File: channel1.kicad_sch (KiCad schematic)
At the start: 58 parts, among them IC1 TLV73325PDBVT, IC2 TLV73312PDBVT, J2 47151-1001, J3 5051101992, U1 TC358742XBG, U2 TPD8S009DSMR, U3 PCA9517ATP, Y1 7C-27.000MBB-T

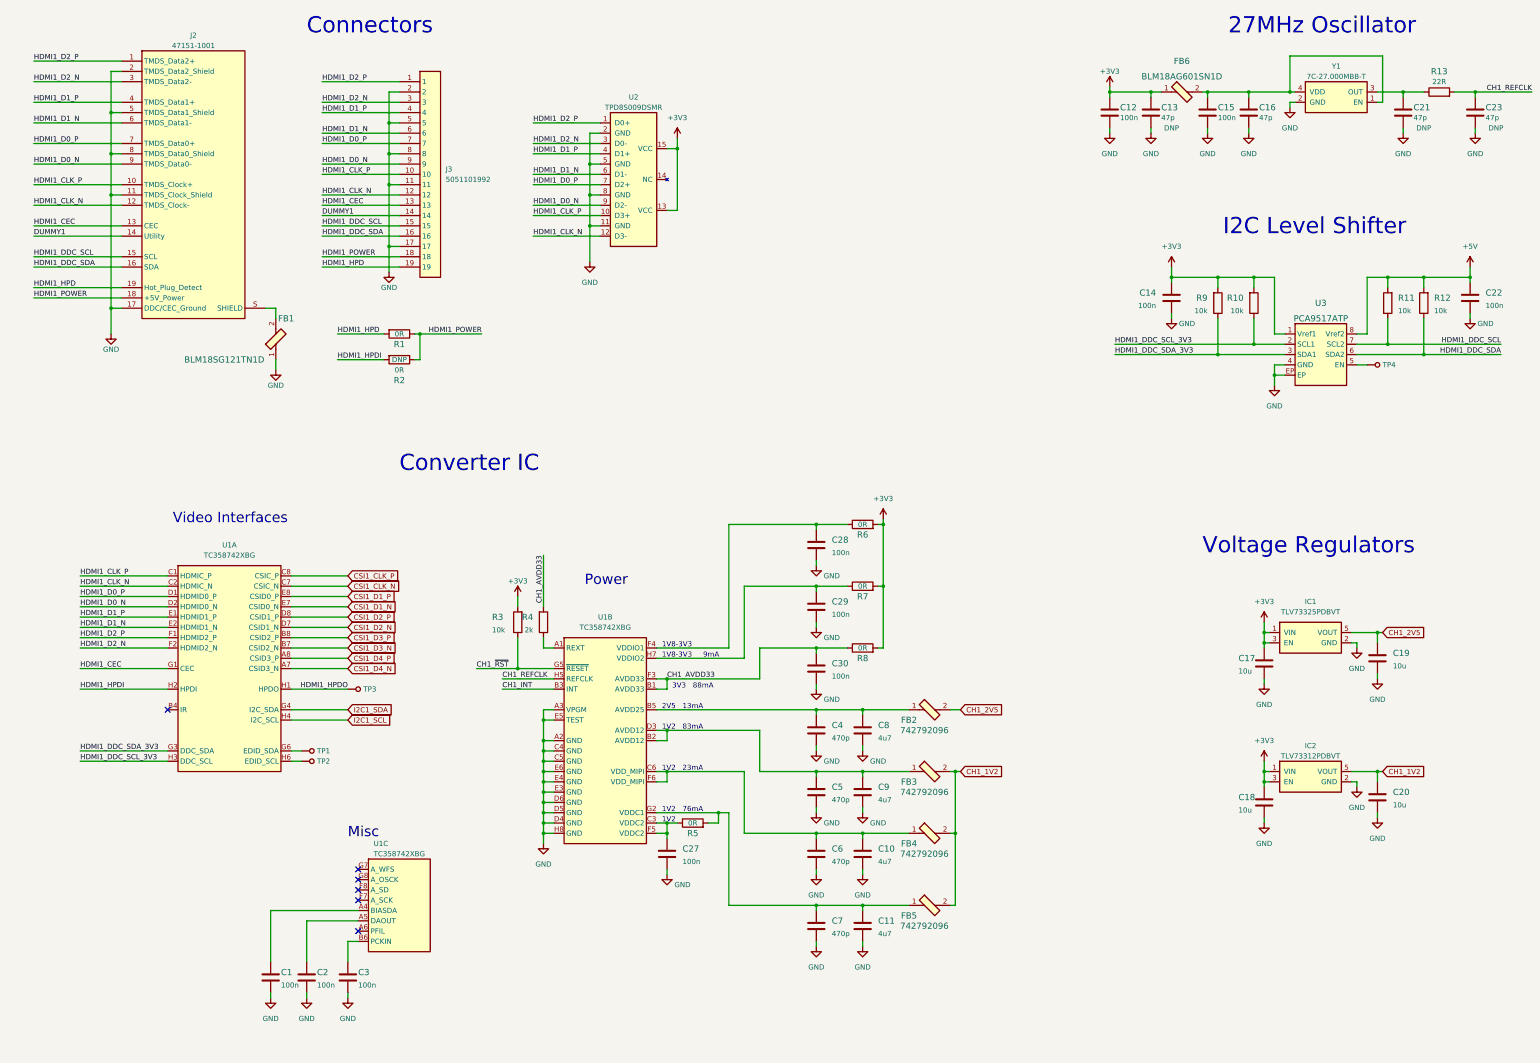
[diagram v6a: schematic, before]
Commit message: Introduce component standardization
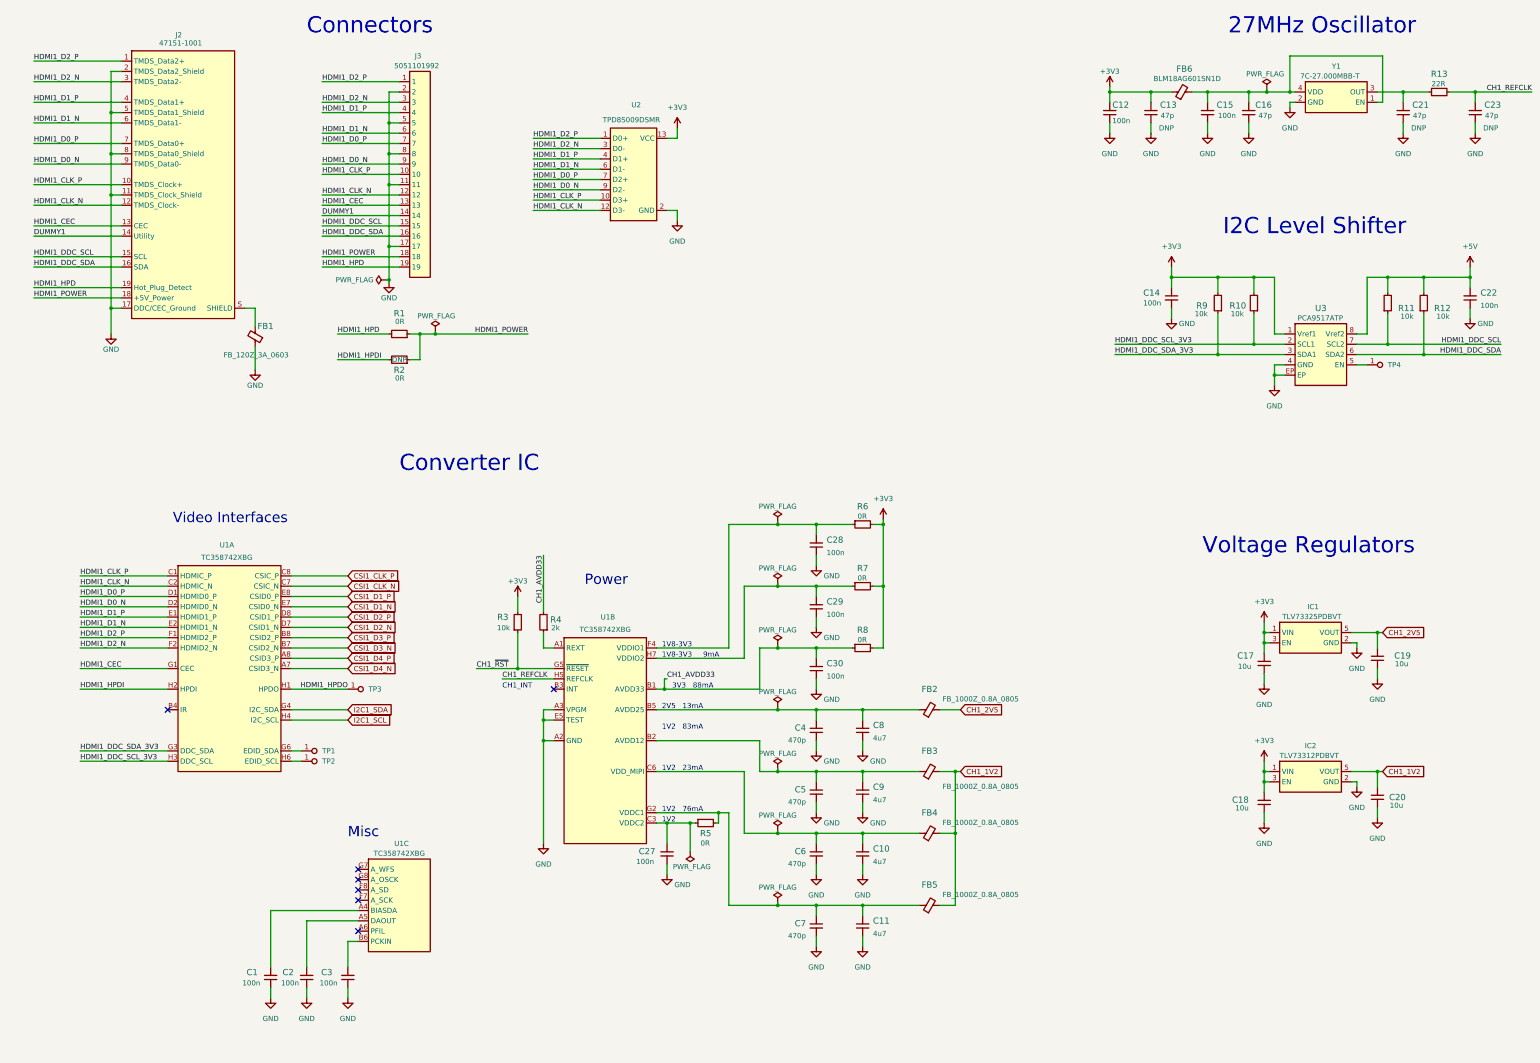
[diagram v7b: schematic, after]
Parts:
- C1, C12, C14, C15, C2, C22, C27, C28, C29, C3, C30: footprint antmicro-hdmi-mipi-bridge-hw-footprints:0402-cap -> antmicro-hdmi-mipi-bridge-hw-footprints:C_0402_1005Metric; Author (none) -> Antmicro; Dielectric (none) -> X5R; License (none) -> Apache-2.0; Voltage (none) -> 50V
- C10, C11, C17, C18, C19, C20, C8, C9: footprint antmicro-hdmi-mipi-bridge-hw-footprints:0603-cap -> antmicro-hdmi-mipi-bridge-hw-footprints:C_0603_1608Metric; Author (none) -> Antmicro; License (none) -> Apache-2.0
- C13, C16, C21, C23: footprint antmicro-hdmi-mipi-bridge-hw-footprints:0402-cap -> antmicro-hdmi-mipi-bridge-hw-footprints:C_0402_1005Metric; Author (none) -> Antmicro; Dielectric (none) -> C0G; License (none) -> Apache-2.0; MPN C0402C470J5GACTU -> GRM1555C1E470JA01D; Manufacturer KEMET -> Murata
- C4, C5, C6, C7: footprint antmicro-hdmi-mipi-bridge-hw-footprints:0402-cap -> antmicro-hdmi-mipi-bridge-hw-footprints:C_0402_1005Metric; Author (none) -> Antmicro; License (none) -> Apache-2.0; Manufacturer WALSIN -> Walsin
- FB1: value BLM18SG121TN1D -> FB_120Z_3A_0603; footprint antmicro-hdmi-mipi-bridge-hw-footprints:0603-res -> antmicro-hdmi-mipi-bridge-hw-footprints:FB_0603_1608Metric; symbol antmicro-hdmi-mipi-bridge-hw:BLM18SG121TN1D -> antmicro-hdmi-mipi-bridge-hw:FB_120Z_3A_0603; Author (none) -> Antmicro; License (none) -> Apache-2.0; Manufacturer Murata Electronics North America -> Murata
- FB2, FB3, FB4, FB5: value 742792096 -> FB_1000Z_0.8A_0805; footprint antmicro-hdmi-mipi-bridge-hw-footprints:0805-res -> antmicro-hdmi-mipi-bridge-hw-footprints:FB_0805_2012Metric; symbol antmicro-hdmi-mipi-bridge-hw:742792096 -> antmicro-hdmi-mipi-bridge-hw:FB_1000Z_0.8A_0805; Author (none) -> Antmicro; License (none) -> Apache-2.0; Manufacturer Wurth Electronic -> Würth Elektronik
- FB6: value BLM18AG601SN1D -> FB_600Z_0.5A_0603; footprint antmicro-hdmi-mipi-bridge-hw-footprints:0603 -> antmicro-hdmi-mipi-bridge-hw-footprints:FB_0603_1608Metric; symbol antmicro-hdmi-mipi-bridge-hw:BLM18AG601SN1D -> antmicro-hdmi-mipi-bridge-hw:FB_600Z_0.5A_0603; Author (none) -> Antmicro; License (none) -> Apache-2.0; Manufacturer Murata Electronics North America -> Murata
- IC1, IC2, J2, J3, U1, U2, Y1: Author (none) -> Antmicro; License (none) -> Apache-2.0
- R1, R2, R5, R6, R7, R8: footprint antmicro-hdmi-mipi-bridge-hw-footprints:0603-res -> antmicro-hdmi-mipi-bridge-hw-footprints:R_0603_1608Metric; Author (none) -> Antmicro; Current (none) -> 1A; License (none) -> Apache-2.0; Manufacturer BOURNS -> Bourns
- R10, R11, R12, R3, R9: footprint antmicro-hdmi-mipi-bridge-hw-footprints:0402-res -> antmicro-hdmi-mipi-bridge-hw-footprints:R_0402_1005Metric; Author (none) -> Antmicro; License (none) -> Apache-2.0; MPN CRCW040210K0FKEDHP -> CR0402-FX-1002GLF; Manufacturer VISHAY -> Bourns; Tolerance (none) -> 1%
- R13: footprint antmicro-hdmi-mipi-bridge-hw-footprints:0402-res -> antmicro-hdmi-mipi-bridge-hw-footprints:R_0402_1005Metric; Author (none) -> Antmicro; License (none) -> Apache-2.0; MPN CRCW040222R0FKED -> CR0402-FX-22R0GLF; Manufacturer VISHAY -> Bourns; Tolerance (none) -> 1%
- R4: footprint antmicro-hdmi-mipi-bridge-hw-footprints:0402-res -> antmicro-hdmi-mipi-bridge-hw-footprints:R_0402_1005Metric; Author (none) -> Antmicro; License (none) -> Apache-2.0; MPN CRCW04022K00FKED -> CR0402-FX-2001GLF; Manufacturer VISHAY -> Bourns; Tolerance (none) -> 1%
- TP1, TP2, TP3, TP4: value TP_SMD_0_75MM -> TP_0.75mm_SMD; footprint antmicro-hdmi-mipi-bridge-hw-footprints:Testpoint_smd_0_75mm -> antmicro-hdmi-mipi-bridge-hw-footprints:TP_SMD_0.75mm; symbol antmicro-hdmi-mipi-bridge-hw:TP_SMD_0_75MM -> antmicro-hdmi-mipi-bridge-hw:TP_0.75mm_SMD; Author (none) -> Antmicro; License (none) -> Apache-2.0
- U3: Author (none) -> Antmicro; License (none) -> Apache-2.0; Manufacturer NXP USA Inc. -> NXP
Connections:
- net +3V3: now also C12.2, C13.2, C17.2, C18.2; no longer C12.1, C13.1, C17.1, C18.1
- net +5V: now also C22.2; no longer C22.1
- net CH1_1V2: now also C20.2; no longer C20.1
- net CH1_2V5: now also C19.2; no longer C19.1
- net CH1_AVDD33: now also C30.2; no longer C30.1
- net CH1_REFCLK: now also C23.2; no longer C23.1
- net GND: now also C1.1, C10.1, C11.1, C12.1, C13.1, C15.1, C16.1, C17.1, C18.1, C19.1, C2.1, C20.1, C21.1, C22.1, C23.1, C27.1, C28.1, C29.1, C3.1, C30.1, C4.2, C5.2, C6.2, C7.2, C8.1, C9.1; no longer C1.2, C10.2, C11.2, C12.2, C13.2, C15.2, C16.2, C17.2, C18.2, C19.2, C2.2, C20.2, C21.2, C22.2, C23.2, C27.2, C28.2, C29.2, C3.2, C30.2, C4.1, C5.1, C6.1, C7.1, C8.2, C9.2
- net at FB4.1, U1.C6 (VDD_MIPI), U1.F6 (VDD_MIPI): now also C10.2, C6.1; no longer C10.1, C6.2
- net at FB5.1, R5.2, U1.G2 (VDDC1): now also C11.2, C7.1; no longer C11.1, C7.2
- net at R5.1, U1.C3 (VDDC2), U1.F5 (VDDC2): now also C27.2; no longer C27.1
- net at U1.A4 (BIASDA): now also C1.2; no longer C1.1
- net at FB2.1, U1.B5 (AVDD25): now also C4.1, C8.2; no longer C4.2, C8.1
- net at FB6.2, Y1.1 (EN), Y1.4 (VDD): now also C15.2, C16.2; no longer C15.1, C16.1
- net at U1.B6 (PCKIN): now also C3.2; no longer C3.1
- net at R7.1, U1.H7 (VDDIO2): now also C29.2; no longer C29.1
- net at R6.1, U1.F4 (VDDIO1): now also C28.2; no longer C28.1
- net at R13.1, Y1.3 (OUT): now also C21.2; no longer C21.1
- net at U1.A5 (DAOUT): now also C2.2; no longer C2.1
- net at FB3.1, U1.B2 (AVDD12), U1.D3 (AVDD12): now also C5.1, C9.2; no longer C5.2, C9.1
- net CH1_INT: no longer names the net of U1.B3 (INT)
- no-connect marks 6 -> 7
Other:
- note added: "CH1_INT"
- title: Antmicro HDMI MIPI Bridge -> HDMI-MIPI Bridge
- moved on the sheet: C1, C10, C11, C12, C13, C14, C15, C16, C17, C18, C19, C2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
